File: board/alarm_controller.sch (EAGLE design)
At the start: 147 parts, among them IC3 AT24C, X1 RJ45-8L21-S, X2 RJ45-8L21-S

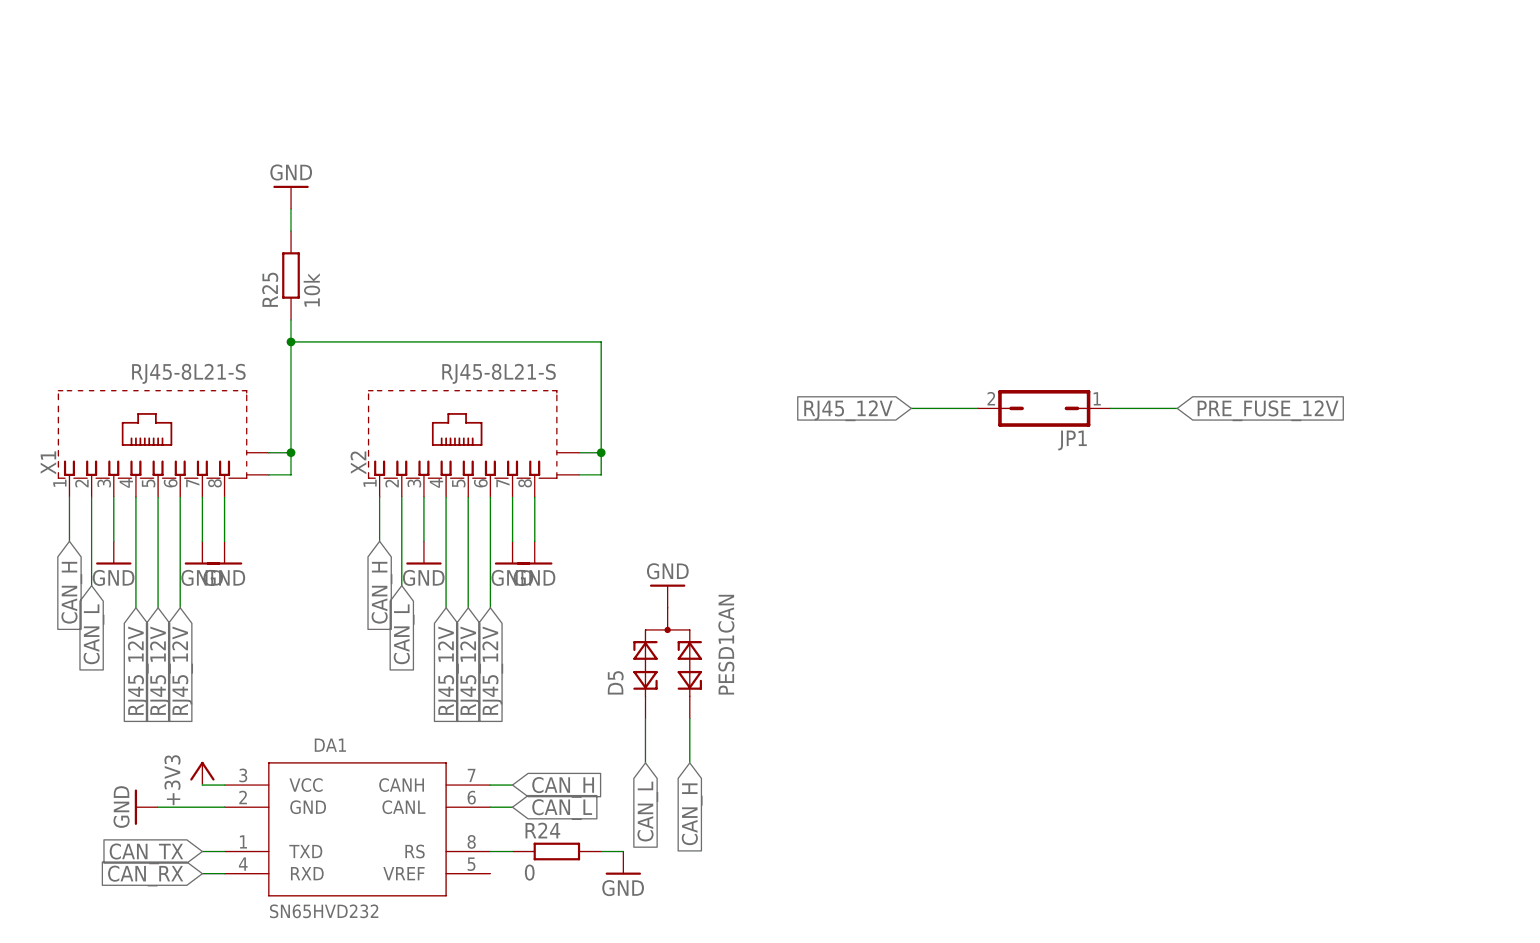
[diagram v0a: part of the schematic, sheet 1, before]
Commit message: change to microfit from rj45
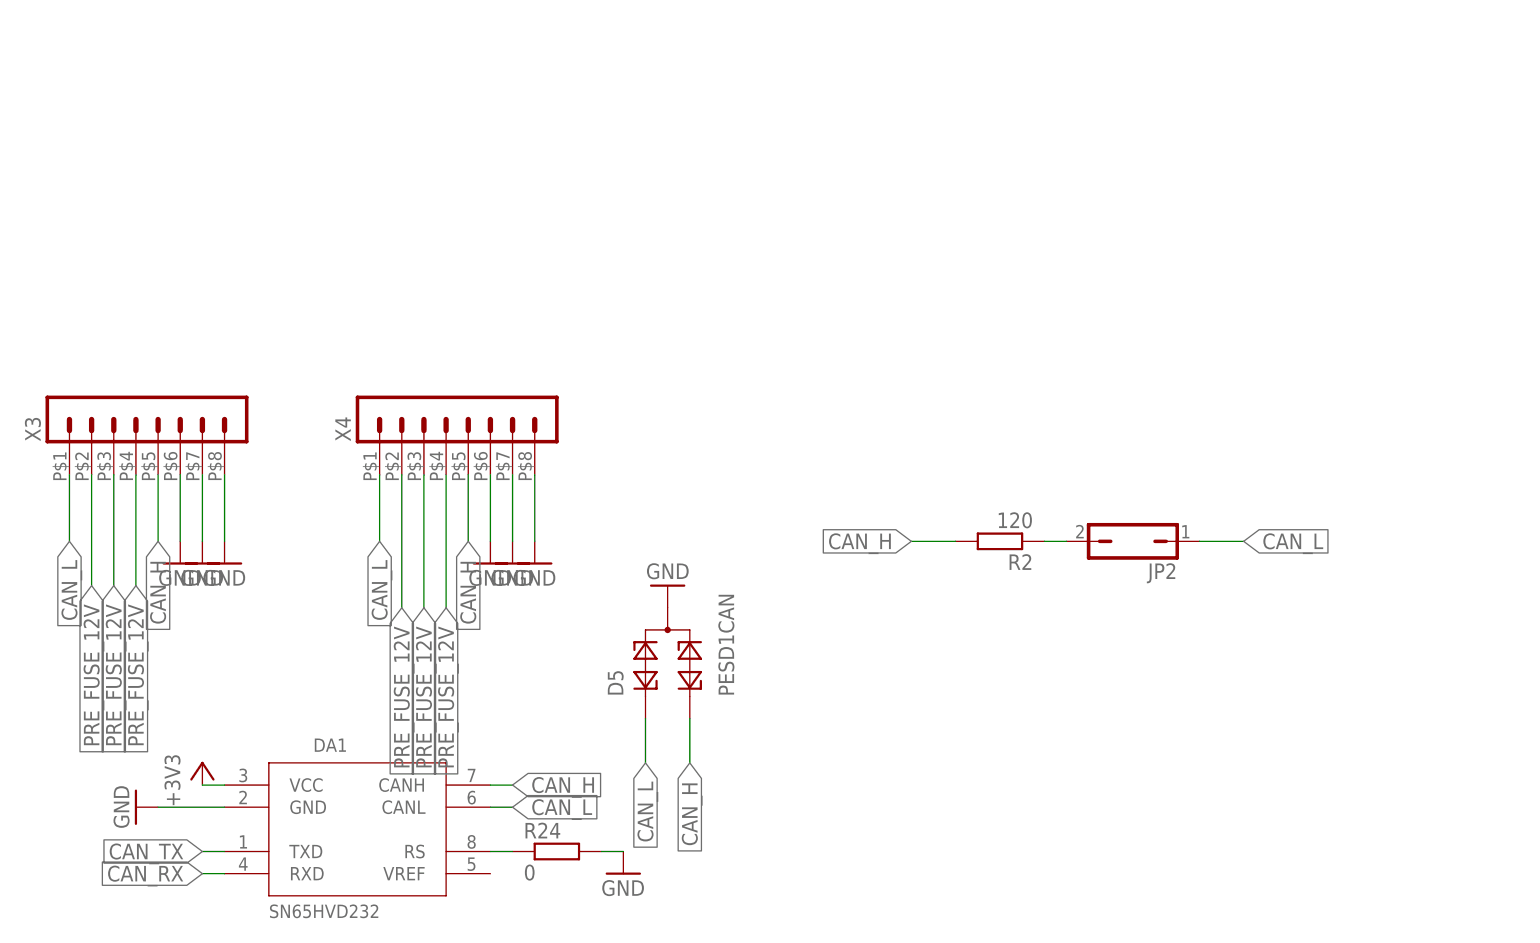
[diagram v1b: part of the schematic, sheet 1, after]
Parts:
- removed GND84: (no value), SparkFun-Connectors:CONN_023.5MM
- removed JP1: (no value), jumper:JP1Q
- removed R25: 10k, rcl:R-EU_R0603
- removed X1, X2: RJ45-8L21-S, con-tycoelectronics:RJ45-8L21-S
- added JP2: (no value), jumper:JP1Q
- added R2: 120, rcl:R-EU_R0603
- added X3, X4: (no value), con-molex-micro-fit-3_0:HEADER_POS8_43045-0812
- added X5: JST-XH-02-PIN-LONG-PAD, Rembrandt Electronics - JST XH Connectors v1-0:JST-XH-02-PIN-LONG-PAD
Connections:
- removed net N$20: R25.1, X1.S@1, X1.S@2, X2.S@1, X2.S@2
- removed net RJ45_12V: JP1.2, X1.4, X1.5, X1.6, X2.4, X2.5, X2.6
- new net N$12: JP2.2, R2.1
- net CAN_H: now also R2.2, X3.5, X4.5; no longer X1.1, X2.1
- net CAN_L: now also JP2.1, X3.1, X4.1; no longer X1.2, X2.2
- net GND: now also X3.6, X3.7, X3.8, X4.6, X4.7, X4.8; no longer R25.2, X1.3, X1.7, X1.8, X2.3, X2.7, X2.8
- net N$10: now also X5-2.S; no longer GND84.2
- net N$11: now also X5-1.S; no longer GND84.1
- net PRE_FUSE_12V: now also X3.2, X3.3, X3.4, X4.2, X4.3, X4.4; no longer JP1.1

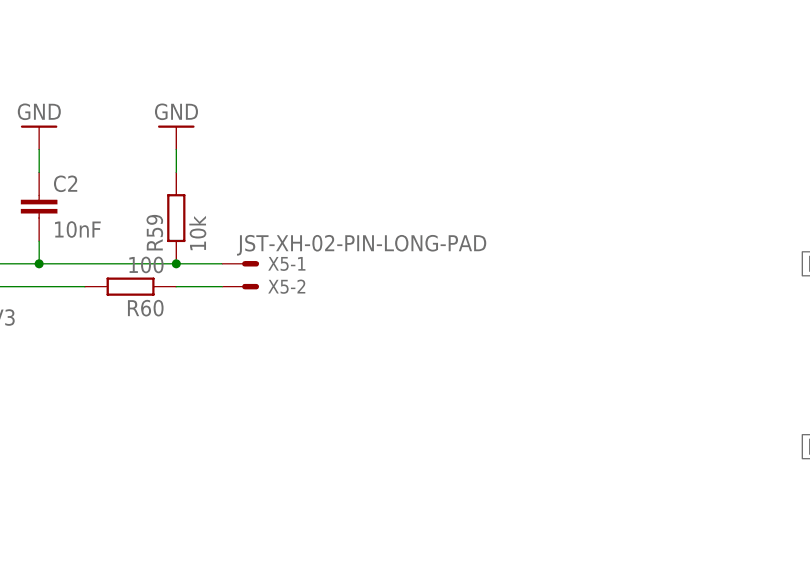
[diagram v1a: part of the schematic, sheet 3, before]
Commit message: change tamper output to regular 3.5mm screw terminal
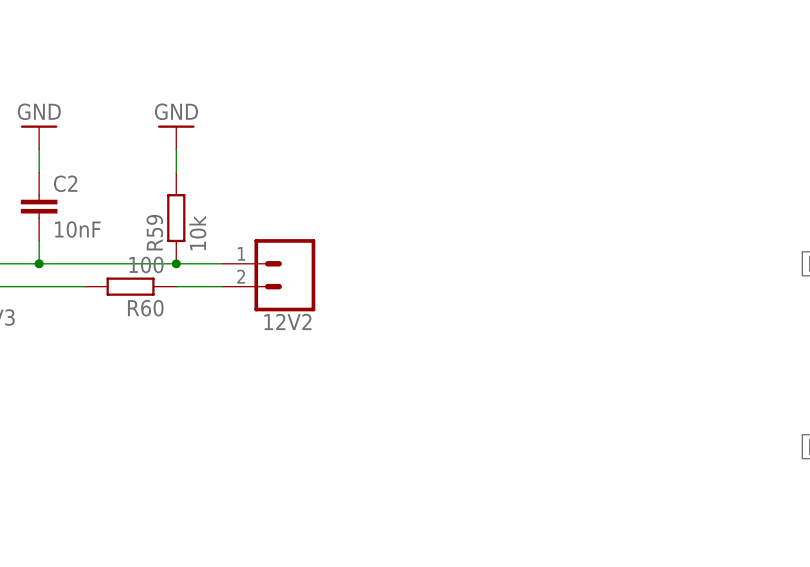
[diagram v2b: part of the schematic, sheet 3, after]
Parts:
- removed X5: JST-XH-02-PIN-LONG-PAD, Rembrandt Electronics - JST XH Connectors v1-0:JST-XH-02-PIN-LONG-PAD
- added 12V2: (no value), SparkFun-Connectors:CONN_023.5MM
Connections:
- net N$10: now also 12V2.2; no longer X5-2.S
- net N$11: now also 12V2.1; no longer X5-1.S
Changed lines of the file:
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@@
 <part name="R2" library="rcl" deviceset="R-EU_" device="R0603" value="120"/>
 <part name="JP2" library="jumper" deviceset="JP1Q" device=""/>
-<part name="X5" library="Rembrandt Electronics - JST XH Connectors v1-0" deviceset="JST-XH-02-PIN" device="-LONG-PAD"/>
+<part name="12V2" library="SparkFun-Connectors" deviceset="CONN_02" device="3.5MM"/>
 </parts>
 <sheets>
@@
 <instance part="GND21" gate="1" x="-35.56" y="91.44" rot="R270"/>
 <instance part="GND22" gate="1" x="-35.56" y="88.9" rot="R270"/>
-<instance part="X5" gate="-2" x="-48.26" y="33.02"/>
-<instance part="X5" gate="-1" x="-48.26" y="35.56"/>
+<instance part="12V2" gate="G$1" x="-43.18" y="35.56" rot="R180"/>
 </instances>
 <busses>
@@
 <pinref part="R60" gate="G$1" pin="1"/>
 <wire x1="-55.88" y1="33.02" x2="-50.8" y2="33.02" width="0.1524" layer="91"/>
-<pinref part="X5" gate="-2" pin="S"/>
+<pinref part="12V2" gate="G$1" pin="2"/>
 </segment>
 </net>
@@
 <wire x1="-76.2" y1="35.56" x2="-71.12" y2="35.56" width="0.1524" layer="91"/>
 <junction x="-71.12" y="35.56"/>
-<pinref part="X5" gate="-1" pin="S"/>
-</segment>
-</net>
+<pinref part="12V2" gate="G$1" pin="1"/>
+</segment>
+</net>

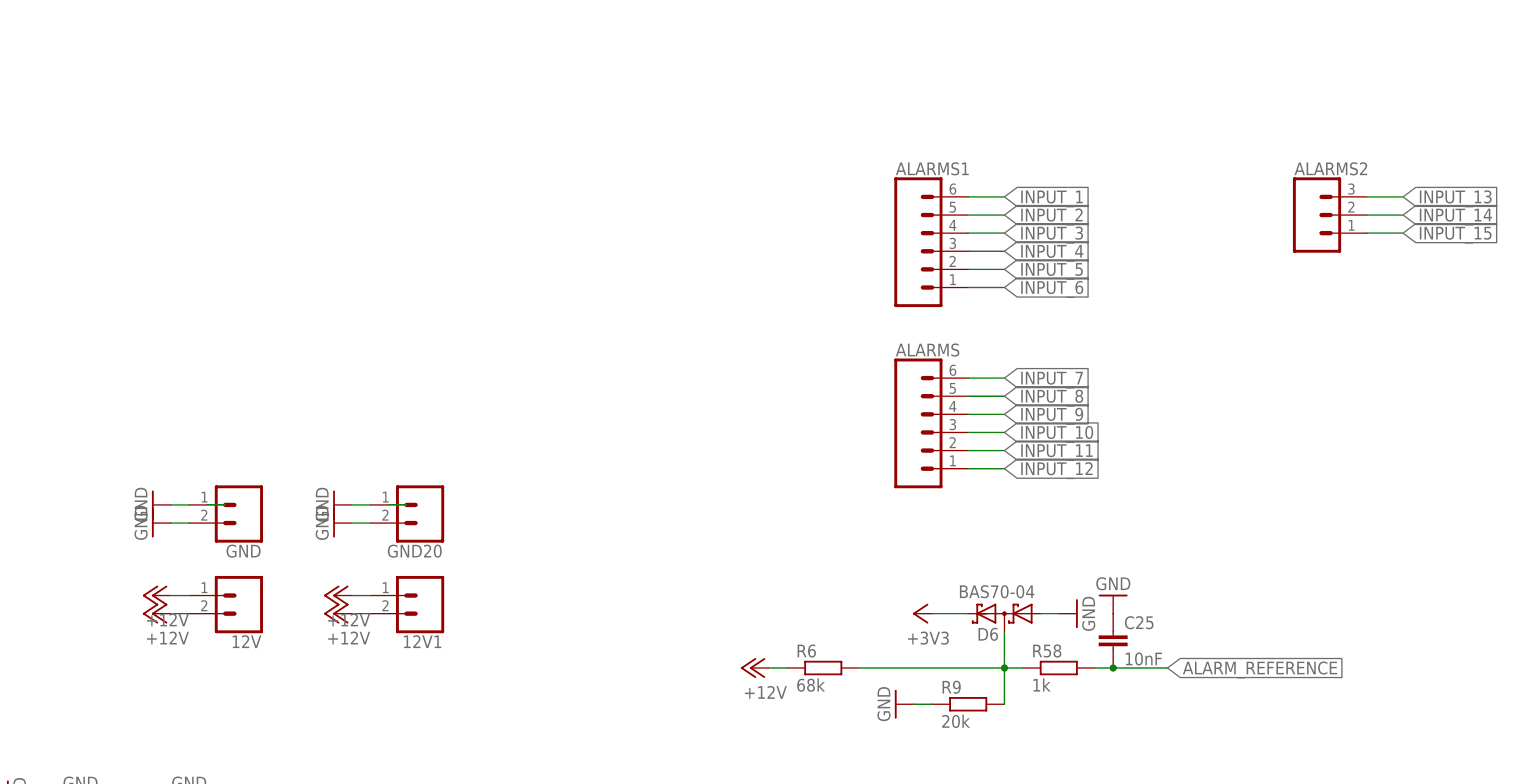
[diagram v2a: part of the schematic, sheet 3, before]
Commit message: redesign voltage divider circuits
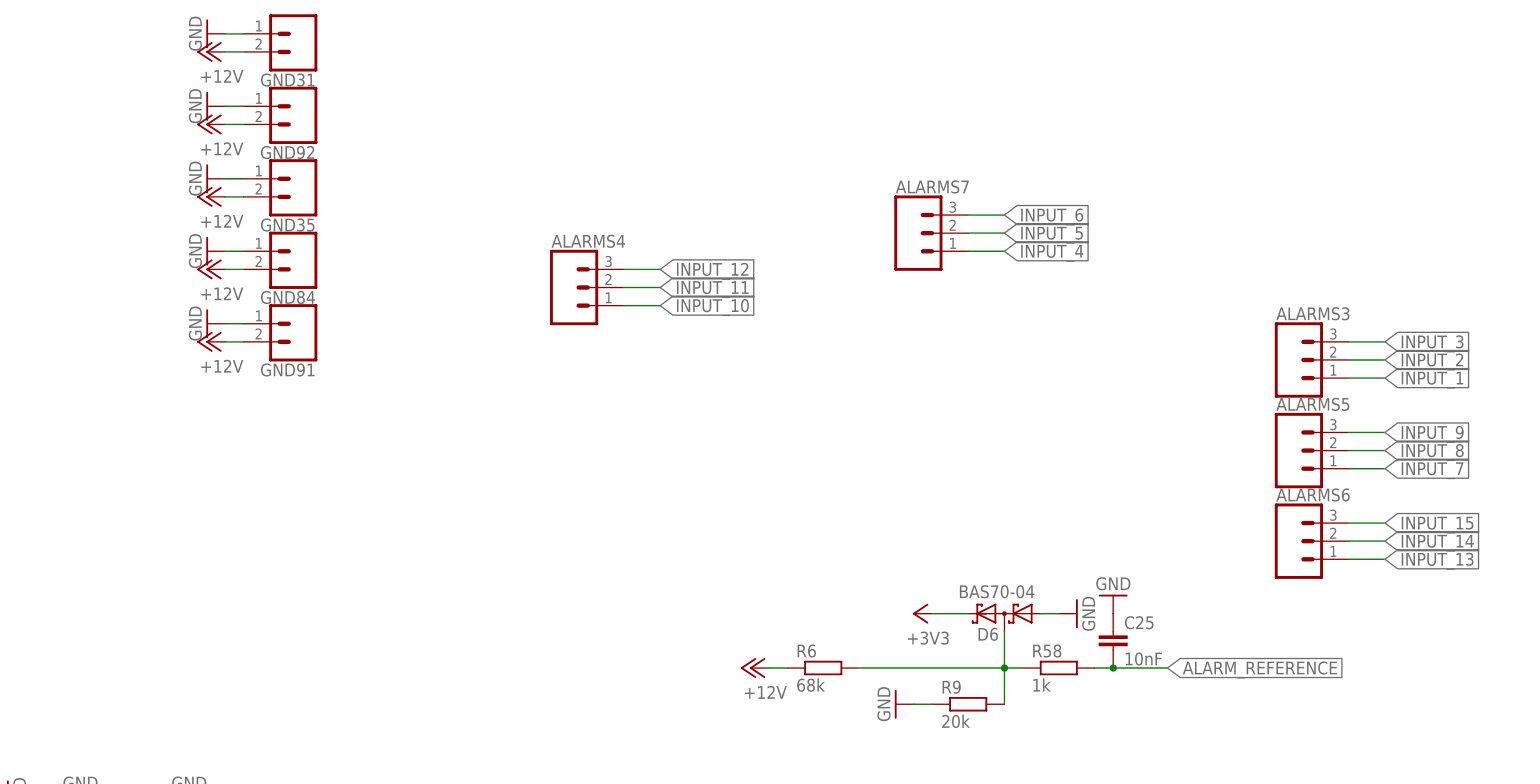
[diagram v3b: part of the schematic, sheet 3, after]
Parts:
- removed 12V, 12V1, GND, GND20: (no value), SparkFun-Connectors:CONN_023.5MM
- removed ALARMS, ALARMS1: (no value), SparkFun-Connectors:CONN_063.5MM-6
- removed ALARMS2: (no value), SparkFun-Connectors:CONN_03SCREW_LOCK
- added ALARMS3, ALARMS4, ALARMS5, ALARMS6, ALARMS7: (no value), SparkFun-Connectors:CONN_03SCREW_LOCK
- added GND31, GND35, GND84, GND91, GND92: (no value), SparkFun-Connectors:CONN_023.5MM
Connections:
- net +12V: now also GND31.2, GND35.2, GND84.2, GND91.2, GND92.2; no longer 12V.1, 12V.2, 12V1.1, 12V1.2
- net GND: now also GND31.1, GND35.1, GND84.1, GND91.1, GND92.1; no longer GND.1, GND.2, GND20.1, GND20.2
- net INPUT_1: now also ALARMS3.1; no longer ALARMS1.6
- net INPUT_10: now also ALARMS4.1; no longer ALARMS.3
- net INPUT_11: now also ALARMS4.2; no longer ALARMS.2
- net INPUT_12: now also ALARMS4.3; no longer ALARMS.1
- net INPUT_13: now also ALARMS6.1; no longer ALARMS2.3
- net INPUT_14: now also ALARMS6.2; no longer ALARMS2.2
- net INPUT_15: now also ALARMS6.3; no longer ALARMS2.1
- net INPUT_2: now also ALARMS3.2; no longer ALARMS1.5
- net INPUT_3: now also ALARMS3.3; no longer ALARMS1.4
- net INPUT_4: now also ALARMS7.1; no longer ALARMS1.3
- net INPUT_5: now also ALARMS7.2; no longer ALARMS1.2
- net INPUT_6: now also ALARMS7.3; no longer ALARMS1.1
- net INPUT_7: now also ALARMS5.1; no longer ALARMS.6
- net INPUT_8: now also ALARMS5.2; no longer ALARMS.5
- net INPUT_9: now also ALARMS5.3; no longer ALARMS.4

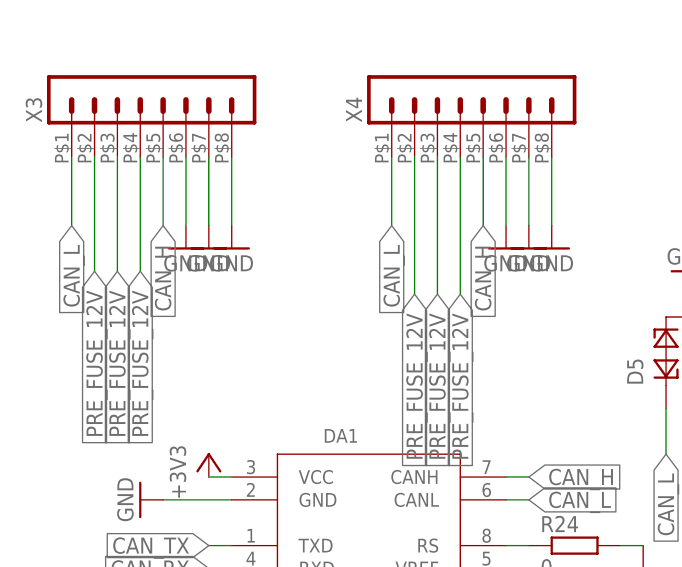
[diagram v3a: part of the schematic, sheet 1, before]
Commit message: update some labels, fix can L and H mixup
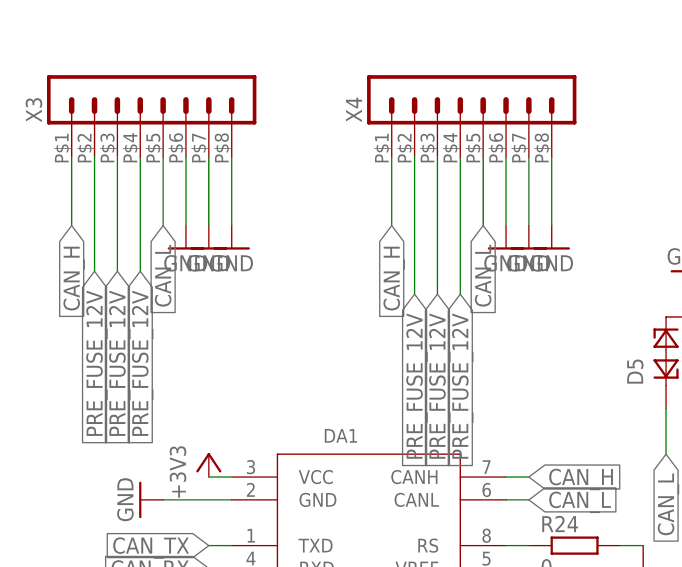
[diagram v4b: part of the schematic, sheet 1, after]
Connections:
- net CAN_H: now also X3.1, X4.1; no longer X3.5, X4.5
- net CAN_L: now also X3.5, X4.5; no longer X3.1, X4.1
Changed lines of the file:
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@@
-</segment>
-<segment>
-<pinref part="X4" gate="G$1" pin="5"/>
-<wire x1="-256.54" y1="-10.16" x2="-256.54" y2="-17.78" width="0.1524" layer="91"/>
-<label x="-256.54" y="-17.78" size="1.778" layer="95" rot="R270" xref="yes"/>
-</segment>
-<segment>
-<pinref part="X3" gate="G$1" pin="5"/>
-<wire x1="-292.1" y1="-10.16" x2="-292.1" y2="-17.78" width="0.1524" layer="91"/>
-<label x="-292.1" y="-17.78" size="1.778" layer="95" rot="R270" xref="yes"/>
 </segment>
 <segment>
@@
 <wire x1="-200.66" y1="-17.78" x2="-205.74" y2="-17.78" width="0.1524" layer="91"/>
 <label x="-205.74" y="-17.78" size="1.778" layer="95" rot="R180" xref="yes"/>
+</segment>
+<segment>
+<wire x1="-302.26" y1="-10.16" x2="-302.26" y2="-17.78" width="0.1524" layer="91"/>
+<label x="-302.26" y="-17.78" size="1.778" layer="95" rot="R270" xref="yes"/>
+<pinref part="X3" gate="G$1" pin="1"/>
+</segment>
+<segment>
+<wire x1="-266.7" y1="-10.16" x2="-266.7" y2="-17.78" width="0.1524" layer="91"/>
+<label x="-266.7" y="-17.78" size="1.778" layer="95" rot="R270" xref="yes"/>
+<pinref part="X4" gate="G$1" pin="1"/>
 </segment>
 </net>
@@
 </segment>
 <segment>
-<wire x1="-266.7" y1="-10.16" x2="-266.7" y2="-17.78" width="0.1524" layer="91"/>
-<label x="-266.7" y="-17.78" size="1.778" layer="95" rot="R270" xref="yes"/>
-<pinref part="X4" gate="G$1" pin="1"/>
-</segment>
-<segment>
-<wire x1="-302.26" y1="-10.16" x2="-302.26" y2="-17.78" width="0.1524" layer="91"/>
-<label x="-302.26" y="-17.78" size="1.778" layer="95" rot="R270" xref="yes"/>
-<pinref part="X3" gate="G$1" pin="1"/>
-</segment>
-<segment>
 <pinref part="JP2" gate="A" pin="1"/>
 <wire x1="-172.72" y1="-17.78" x2="-167.64" y2="-17.78" width="0.1524" layer="91"/>
 <label x="-167.64" y="-17.78" size="1.778" layer="95" xref="yes"/>
 </segment>
+<segment>
+<pinref part="X3" gate="G$1" pin="5"/>
+<wire x1="-292.1" y1="-10.16" x2="-292.1" y2="-17.78" width="0.1524" layer="91"/>
+<label x="-292.1" y="-17.78" size="1.778" layer="95" rot="R270" xref="yes"/>
+</segment>
+<segment>
+<pinref part="X4" gate="G$1" pin="5"/>
+<wire x1="-256.54" y1="-10.16" x2="-256.54" y2="-17.78" width="0.1524" layer="91"/>
+<label x="-256.54" y="-17.78" size="1.778" layer="95" rot="R270" xref="yes"/>
+</segment>
 </net>
